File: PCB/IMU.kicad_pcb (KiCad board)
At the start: 2 copper layers, 77.2 x 49.8 mm, 68 parts, among them IC1 STM32F405VGT, IC2 ADP3335ARMZ-3.3, IC3 ADP3335ARMZ-5, IC4 MS5611-01BA03, P1 UART1, P2 SWD, P3 UART2, P4 SPI, P5 BATTERY, P6 USB_OTG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

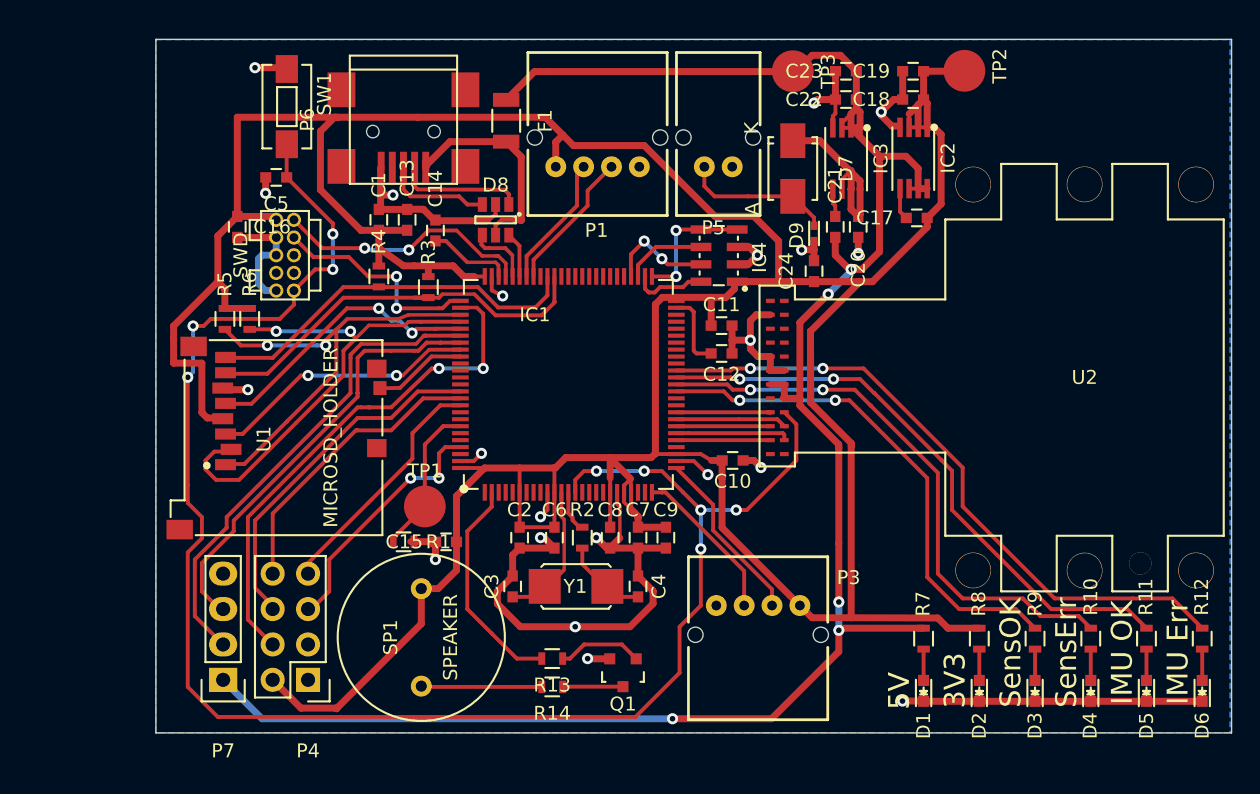
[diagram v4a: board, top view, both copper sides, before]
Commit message: Added an MPU-9250 on the same SPI bus as the ADIS sensor. The PCB routing is a first draft and I may tweak it a bit further.
I had to change the track spacing tolerance from 0.2mm to 0.19mm to be able to wire up the sensor.
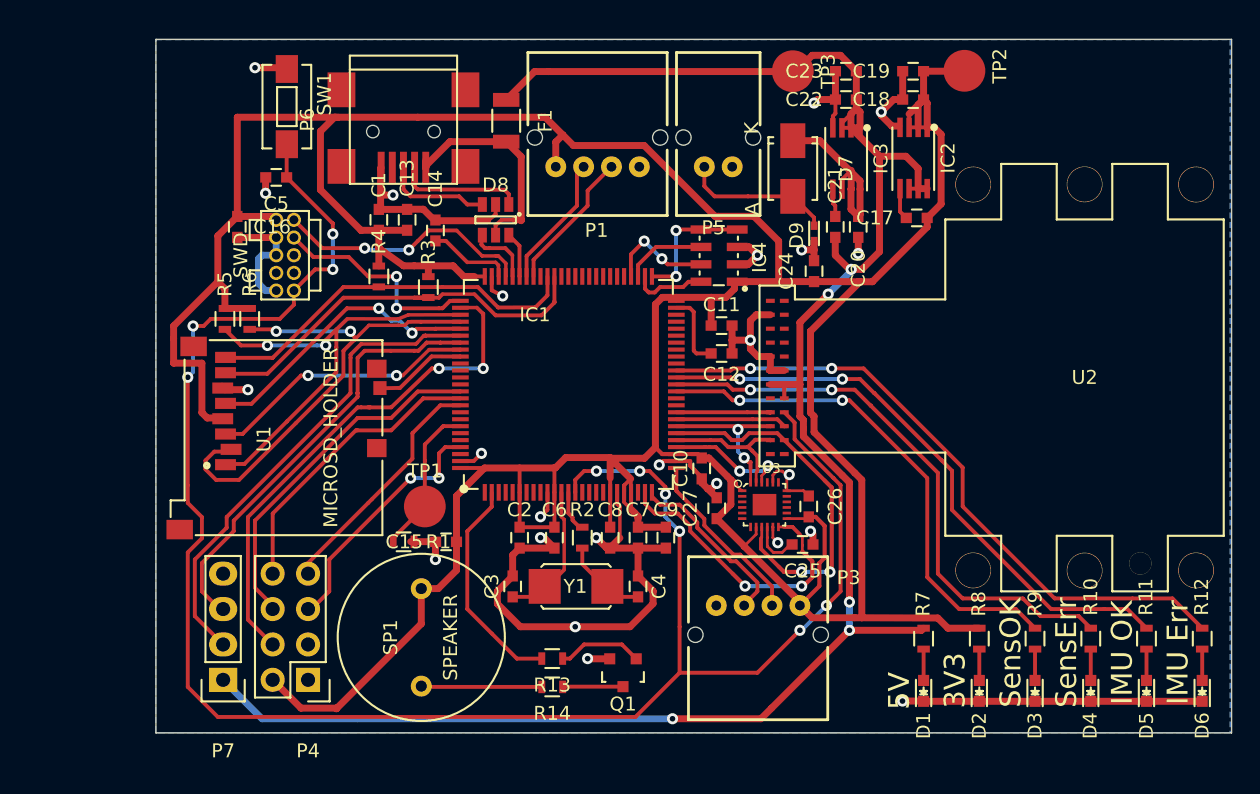
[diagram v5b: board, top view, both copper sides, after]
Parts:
- added C25: 100n, Capacitors_SMD:C_0603, F.Cu at (198.3, 114.5)
- added C26: 10n, Capacitors_SMD:C_0603, F.Cu at (198.8, 111.8)
- added C27: 100n, Capacitors_SMD:C_0603, F.Cu at (192.2, 111.9)
- added U3: MOTION/POSITION-MPU-9250(QFN24), IMU:QFN24G-0.4-3X3MM, F.Cu at (195.6, 111.6)
- moved C10 2.29 mm to (191.1, 109.0), turned to 270 degrees
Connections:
- net /IntertialSensors/IRQ renamed /IntertialSensors/ADIS_IRQ
- net SPI1_NSS renamed /IntertialSensors/~ADIS_SS
- IC1 pad 24: Net-(IC1-Pad24) -> /IntertialSensors/MPU_IRQ
- IC1 pad 29: Net-(IC1-Pad29) -> /IntertialSensors/~MPU_SS
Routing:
- net /IntertialSensors/MPU_IRQ: track 0.00 -> 21.0 mm, vias 0 -> 2
- net SPI1_MISO: track 8.19 -> 26.6 mm, vias 0 -> 2
- net ~RST: track 123.1 -> 137.7 mm, vias 9 -> 10
- net GND: track 129.8 -> 139.2 mm, vias 21 -> 24
- net /IntertialSensors/~MPU_SS: track 0.00 -> 8.93 mm, vias 0 -> 2
- net +3V3: track 295.3 -> 303.7 mm
- net SPI1_MOSI: track 6.75 -> 11.3 mm, vias 0 -> 2
- net Net-(C25-Pad2): track 0.00 -> 3.59 mm
- net SPI1_SCK: track 6.75 -> 10.3 mm
- net USART2_TX: track 11.5 -> 12.9 mm
- net +5V: track 144.0 -> 143.4 mm
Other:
- net class Default: clearance 0.2 -> 0.19
- net class Power: clearance 0.2 -> 0.19
- rule trace_clearance: 0.2 -> 0.19

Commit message: Add silkscreen to PCB
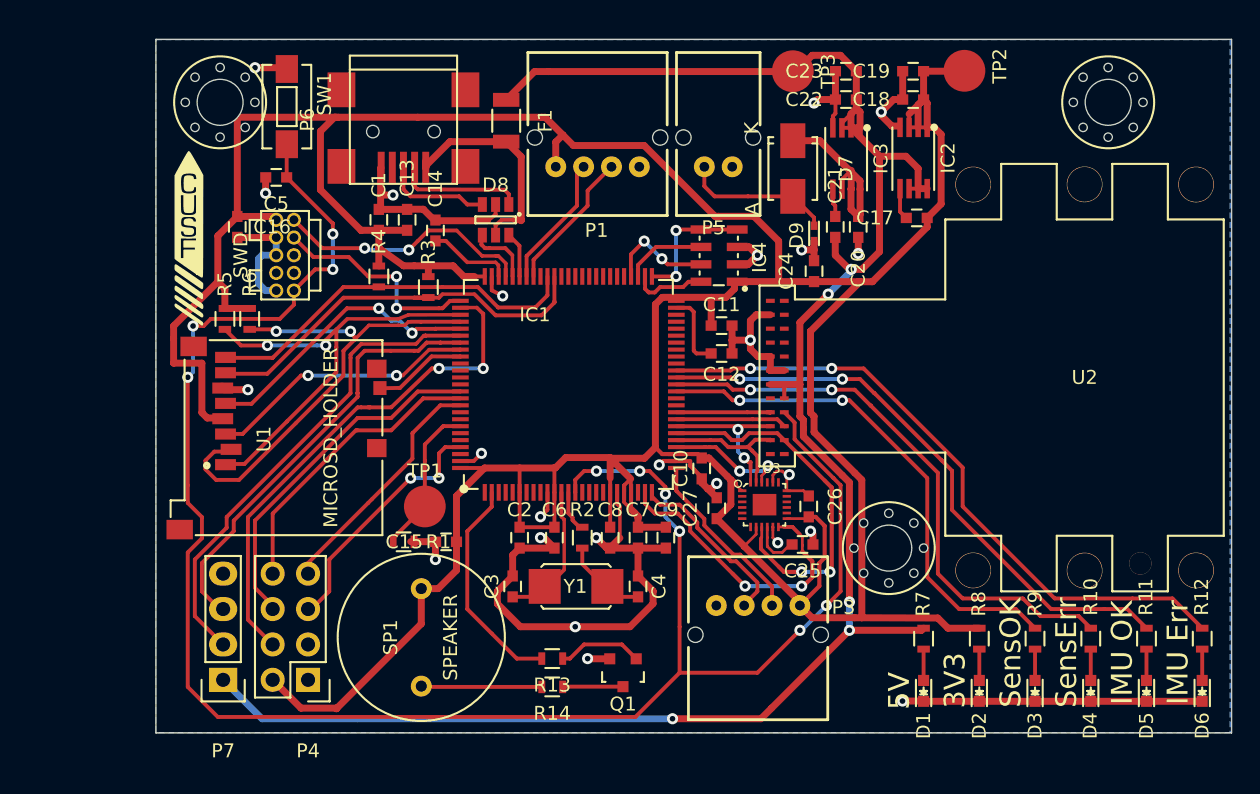
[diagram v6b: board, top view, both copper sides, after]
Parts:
- added G***: LOGO, IMU:cusf_logo_full, F.Cu at (201.5, 106.5)
- added G***: LOGO, IMU:cusf_logo_small, F.Cu at (154.2, 92.5)
- added M3_MOUNT: VAL**, IMU:M3_MOUNT, F.Cu at (220.2, 82.8)
- added M3_MOUNT: VAL**, IMU:M3_MOUNT, F.Cu at (156.5, 82.8)
- added M3_MOUNT: VAL**, IMU:M3_MOUNT, F.Cu at (204.5, 114.8)
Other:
- board text added: "A Clowes B Wong E Eide G Brooks J Brewster J Timmins L Cockerton R Taylor-Davies R Wareham S Ober"
- board text added: "www.cusf.co.uk"

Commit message: Fix PCB mounting holes
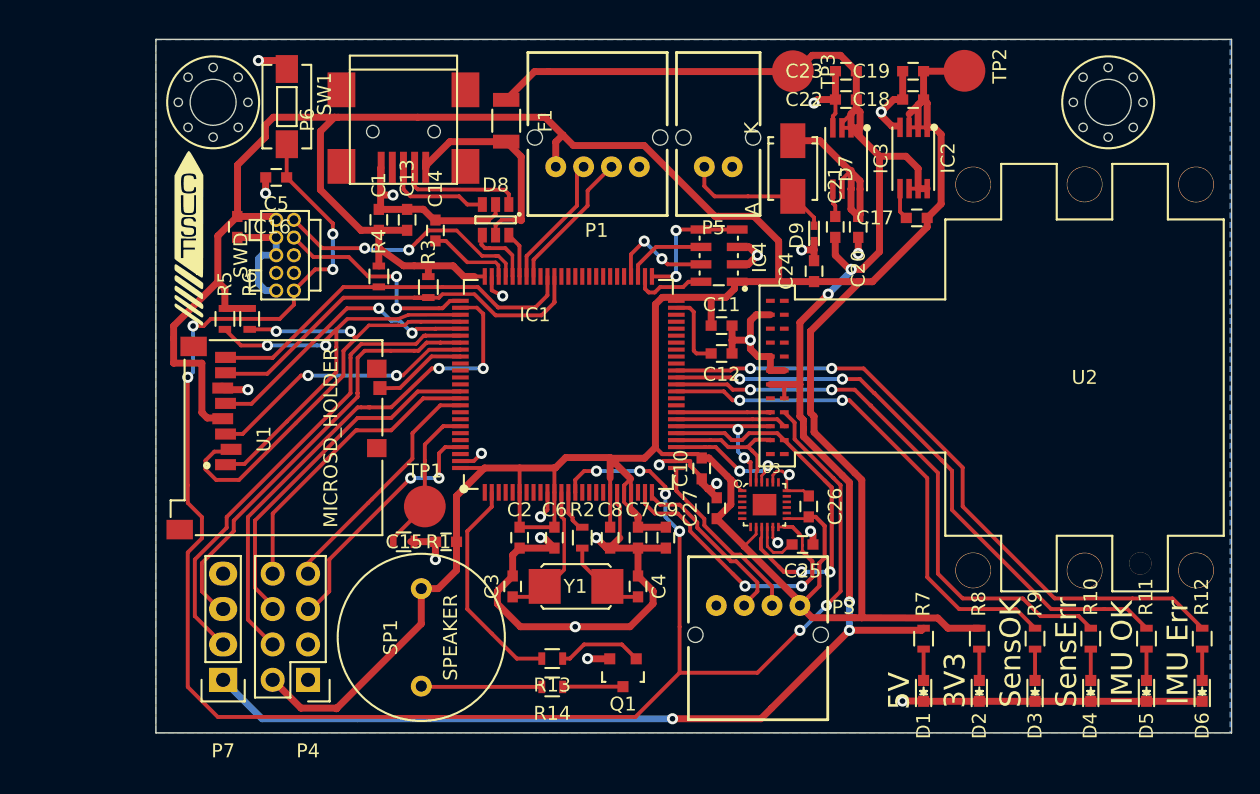
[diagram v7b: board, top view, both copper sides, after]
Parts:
- removed the M3_MOUNT at (204.5, 114.8)
- moved M3_MOUNT 0.50 mm to (156.0, 82.8)
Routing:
- net +3V3: track 303.7 -> 302.0 mm
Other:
- rule trace_min: 0.2 -> 0.19
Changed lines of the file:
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@@
     (thickness 1.6)
     (drawings 12)
-    (tracks 1030)
+    (tracks 1035)
     (zones 0)
-    (modules 77)
+    (modules 76)
     (nets 137)
   )
   (page A4)
   (layers
-    (0 F.Cu signal hide)
-    (31 B.Cu signal hide)
+    (0 F.Cu signal)
+    (31 B.Cu signal)
     (32 B.Adhes user hide)
     (33 F.Adhes user hide)
@@
     (zone_clearance 0.508)
     (zone_45_only no)
-    (trace_min 0.2)
+    (trace_min 0.19)
     (segment_width 0.2)
     (edge_width 0.1)
@@
   )
   (module IMU:M3_MOUNT (layer F.Cu)
-    (at 156.5 82.75)
-    (fp_text reference M3_MOUNT (at 0 -4) (layer F.SilkS) hide
-      (effects (font (size 1 1) (thickness 0.15)))
-    )
-    (fp_text value VAL** (at 0 4) (layer F.SilkS) hide
-      (effects (font (size 1 1) (thickness 0.15)))
-    )
-    (fp_circle (center 0 0) (end 3.3 0) (layer F.SilkS) (width 0.15))
-    (pad "" np_thru_hole circle (at 0 0) (size 3.3 3.3) (drill 3.3) (layers *.Cu *.Mask F.Paste F.SilkS)
-      (solder_mask_margin 1.5) (clearance 1.65))
-    (pad "" np_thru_hole circle (at 0 -2.5) (size 0.6 0.6) (drill 0.6) (layers *.Cu *.Mask F.SilkS))
-    (pad "" np_thru_hole circle (at 2.5 0) (size 0.6 0.6) (drill 0.6) (layers *.Cu *.Mask F.SilkS))
-    (pad "" np_thru_hole circle (at 0 2.5) (size 0.6 0.6) (drill 0.6) (layers *.Cu *.Mask F.SilkS))
-    (pad "" np_thru_hole circle (at -2.5 0) (size 0.6 0.6) (drill 0.6) (layers *.Cu *.Mask F.SilkS))
-    (pad "" np_thru_hole circle (at -1.8 -1.8) (size 0.6 0.6) (drill 0.6) (layers *.Cu *.Mask F.SilkS))
-    (pad "" np_thru_hole circle (at 1.8 -1.8) (size 0.6 0.6) (drill 0.6) (layers *.Cu *.Mask F.SilkS))
-    (pad "" np_thru_hole circle (at -1.8 1.8) (size 0.6 0.6) (drill 0.6) (layers *.Cu *.Mask F.SilkS))
-    (pad "" np_thru_hole circle (at 1.8 1.8) (size 0.6 0.6) (drill 0.6) (layers *.Cu *.Mask F.SilkS))
-  )
-  (module IMU:M3_MOUNT (layer F.Cu)
-    (at 204.5 114.75)
+    (at 156 82.75)
     (fp_text reference M3_MOUNT (at 0 -4) (layer F.SilkS) hide
       (effects (font (size 1 1) (thickness 0.15)))
@@
     (effects (font (size 1.5 1.5) (thickness 0.3)))
   )
+  (segment (start 164.719 83.82) (end 160.32 83.82) (width 0.5) (layer F.Cu) (net 1))
+  (segment (start 157.75 87.25) (end 157.75 90.928) (width 0.5) (layer F.Cu) (net 1))
+  (segment (start 159.75 85.25) (end 157.75 87.25) (width 0.5) (layer F.Cu) (net 1))
+  (segment (start 159.75 84.39) (end 159.75 85.25) (width 0.5) (layer F.Cu) (net 1))
+  (segment (start 160.32 83.82) (end 159.75 84.39) (width 0.5) (layer F.Cu) (net 1))
+  (segment (start 157.75 90.928) (end 157.734 90.944) (width 0.5) (layer F.Cu) (net 1))
   (segment (start 198.12 118.618) (end 194.1195 114.6175) (width 0.5) (layer F.Cu) (net 1))
   (segment (start 199.898 113.157) (end 199.898 115.443) (width 0.3) (layer F.Cu) (net 1))
@@
   (segment (start 186 110.75) (end 185.975 109.775) (width 0.28) (layer F.Cu) (net 1))
   (segment (start 164.846 126.238) (end 164.846 126.238) (width 0.5) (layer F.Cu) (net 1))
-  (segment (start 157.734 90.944) (end 157.734 83.82) (width 0.5) (layer F.Cu) (net 1))
-  (segment (start 157.734 83.82) (end 164.846 83.82) (width 0.5) (layer F.Cu) (net 1))
   (segment (start 164.719 83.82) (end 163.703 84.836) (width 0.5) (layer F.Cu) (net 1))
   (segment (start 164.973 83.82) (end 164.719 83.82) (width 0.5) (layer F.Cu) (net 1))
@@
   (segment (start 184.5 110.75) (end 184.5 113.25) (width 0.28) (layer F.Cu) (net 1))
   (segment (start 180.5 110.75) (end 180.5 113.25) (width 0.28) (layer F.Cu) (net 1))
+  (segment (start 159.25 79.75) (end 160.682 79.75) (width 0.5) (layer F.Cu) (net 2))
+  (via (at 159.25 79.75) (size 0.8) (drill 0.4) (layers F.Cu B.Cu) (net 2))
+  (segment (start 160.682 79.75) (end 161.29 80.358) (width 0.5) (layer F.Cu) (net 2))
   (segment (start 199.0605 114.4905) (end 199.0605 113.7165) (width 0.5) (layer F.Cu) (net 2))
   (via (at 198.882 113.538) (size 0.8) (drill 0.4) (layers F.Cu B.Cu) (net 2))
@@
   (via (at 159.766 89.281) (size 0.8) (drill 0.4) (layers F.Cu B.Cu) (net 2))
   (segment (start 161.29 80.358) (end 161.196 80.264) (width 0.5) (layer F.Cu) (net 2))
-  (segment (start 161.196 80.264) (end 159.004 80.264) (width 0.5) (layer F.Cu) (net 2))
-  (via (at 159.004 80.264) (size 0.8) (drill 0.4) (layers F.Cu B.Cu) (net 2))
   (segment (start 168.91 89.408) (end 168.021 89.408) (width 0.5) (layer F.Cu) (net 2))
   (via (at 168.91 89.408) (size 0.8) (drill 0.4) (layers F.Cu B.Cu) (net 2))
